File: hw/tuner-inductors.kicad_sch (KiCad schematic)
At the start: 23 parts, among them K7713 G5Q-14-05, K7714 G5Q-14-05, K7715 G5Q-14-05, K7716 G5Q-14-05, K7717 G5Q-14-05, K7718 G5Q-14-05, K7719 G5Q-14-05, U7745 TPIC6C595PWR

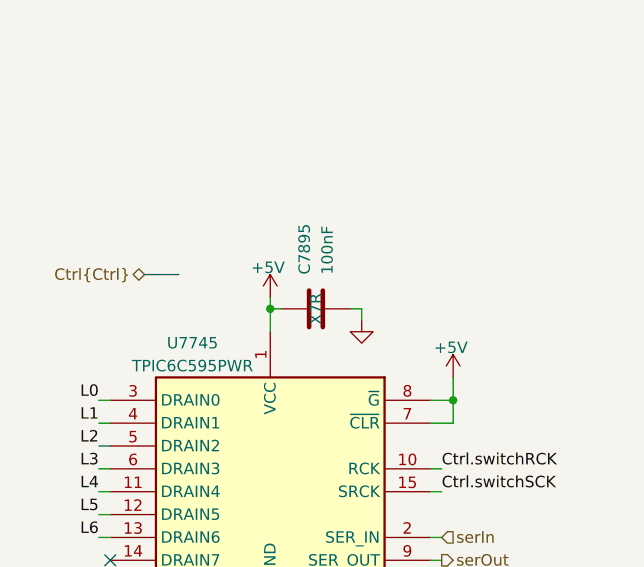
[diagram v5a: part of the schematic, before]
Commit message: All symbols and footprints seem right now, and schematic again imports into PCB without error
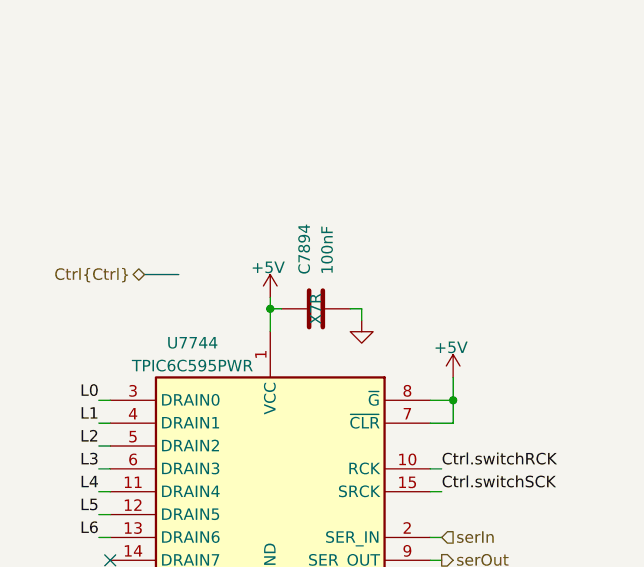
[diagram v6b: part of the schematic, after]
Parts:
- renumbered C7895 to C7894, U7745 to U7744
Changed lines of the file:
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@@
 		(dnp no)
 		(fields_autoplaced yes)
-		(property "Reference" "#PWR07990"
+		(property "Reference" "#PWR07989"
 			(at 39.37 205.74 0)
 			(effects
@@
 			(project "NexRig"
 				(path "/8ae46c04-d01a-4756-8774-512b694bfaff/2406d03c-531b-4eaf-8b4b-4b266b9d0f2b/99bbdde6-e23e-4e3f-9a6c-8b2d863ddc64/99065376-3804-4997-bf5b-41fcd6e501f1"
-					(reference "#PWR07990")
+					(reference "#PWR07989")
 					(unit 1)
 				)
@@
 		(on_board yes)
 		(dnp no)
-		(property "Reference" "#PWR07995"
+		(property "Reference" "#PWR07994"
 			(at 149.86 68.58 0)
 			(effects
@@
 			(project "NexRig"
 				(path "/8ae46c04-d01a-4756-8774-512b694bfaff/2406d03c-531b-4eaf-8b4b-4b266b9d0f2b/99bbdde6-e23e-4e3f-9a6c-8b2d863ddc64/99065376-3804-4997-bf5b-41fcd6e501f1"
-					(reference "#PWR07995")
+					(reference "#PWR07994")
 					(unit 1)
 				)
@@
 		(dnp no)
 		(fields_autoplaced yes)
-		(property "Reference" "#PWR07991"
+		(property "Reference" "#PWR07990"
 			(at 49.53 170.18 0)
 			(effects
@@
 			(project "NexRig"
 				(path "/8ae46c04-d01a-4756-8774-512b694bfaff/2406d03c-531b-4eaf-8b4b-4b266b9d0f2b/99bbdde6-e23e-4e3f-9a6c-8b2d863ddc64/99065376-3804-4997-bf5b-41fcd6e501f1"
-					(reference "#PWR07991")
+					(reference "#PWR07990")
 					(unit 1)
 				)
@@
 		(on_board yes)
 		(dnp no)
-		(property "Reference" "#PWR07992"
+		(property "Reference" "#PWR07991"
 			(at 59.69 173.99 0)
 			(effects
@@
 			(project "NexRig"
 				(path "/8ae46c04-d01a-4756-8774-512b694bfaff/2406d03c-531b-4eaf-8b4b-4b266b9d0f2b/99bbdde6-e23e-4e3f-9a6c-8b2d863ddc64/99065376-3804-4997-bf5b-41fcd6e501f1"
-					(reference "#PWR07992")
+					(reference "#PWR07991")
 					(unit 1)
 				)
@@
 		(on_board yes)
 		(dnp no)
-		(property "Reference" "C7895"
+		(property "Reference" "C7894"
 			(at 43.1799 158.75 0)
 			(effects
@@
 			(project "NexRig"
 				(path "/8ae46c04-d01a-4756-8774-512b694bfaff/2406d03c-531b-4eaf-8b4b-4b266b9d0f2b/99bbdde6-e23e-4e3f-9a6c-8b2d863ddc64/99065376-3804-4997-bf5b-41fcd6e501f1"
-					(reference "C7895")
+					(reference "C7894")
 					(unit 1)
 				)
@@
 		(on_board yes)
 		(dnp no)
-		(property "Reference" "U7745"
+		(property "Reference" "U7744"
 			(at 30.734 166.37 0)
 			(effects
@@
 			(project "NexRig"
 				(path "/8ae46c04-d01a-4756-8774-512b694bfaff/2406d03c-531b-4eaf-8b4b-4b266b9d0f2b/99bbdde6-e23e-4e3f-9a6c-8b2d863ddc64/99065376-3804-4997-bf5b-41fcd6e501f1"
-					(reference "U7745")
+					(reference "U7744")
 					(unit 1)
 				)
@@
 		(on_board yes)
 		(dnp no)
-		(property "Reference" "#PWR07989"
+		(property "Reference" "#PWR07988"
 			(at 39.37 165.1 0)
 			(effects
@@
 			(project "NexRig"
 				(path "/8ae46c04-d01a-4756-8774-512b694bfaff/2406d03c-531b-4eaf-8b4b-4b266b9d0f2b/99bbdde6-e23e-4e3f-9a6c-8b2d863ddc64/99065376-3804-4997-bf5b-41fcd6e501f1"
-					(reference "#PWR07989")
+					(reference "#PWR07988")
 					(unit 1)
 				)
@@
 		(on_board yes)
 		(dnp no)
-		(property "Reference" "#PWR07998"
+		(property "Reference" "#PWR07997"
 			(at 226.06 68.58 0)
 			(effects
@@
 			(project "NexRig"
 				(path "/8ae46c04-d01a-4756-8774-512b694bfaff/2406d03c-531b-4eaf-8b4b-4b266b9d0f2b/99bbdde6-e23e-4e3f-9a6c-8b2d863ddc64/99065376-3804-4997-bf5b-41fcd6e501f1"
-					(reference "#PWR07998")
+					(reference "#PWR07997")
 					(unit 1)
 				)
@@
 		(on_board yes)
 		(dnp no)
-		(property "Reference" "#PWR07996"
+		(property "Reference" "#PWR07995"
 			(at 175.26 68.58 0)
 			(effects
@@
 			(project "NexRig"
 				(path "/8ae46c04-d01a-4756-8774-512b694bfaff/2406d03c-531b-4eaf-8b4b-4b266b9d0f2b/99bbdde6-e23e-4e3f-9a6c-8b2d863ddc64/99065376-3804-4997-bf5b-41fcd6e501f1"
-					(reference "#PWR07996")
+					(reference "#PWR07995")
 					(unit 1)
 				)
@@
 		(on_board yes)
 		(dnp no)
-		(property "Reference" "#PWR07999"
+		(property "Reference" "#PWR07998"
 			(at 251.46 68.58 0)
 			(effects
@@
 			(project "NexRig"
 				(path "/8ae46c04-d01a-4756-8774-512b694bfaff/2406d03c-531b-4eaf-8b4b-4b266b9d0f2b/99bbdde6-e23e-4e3f-9a6c-8b2d863ddc64/99065376-3804-4997-bf5b-41fcd6e501f1"
-					(reference "#PWR07999")
+					(reference "#PWR07998")
 					(unit 1)
 				)
@@
 		(on_board yes)
 		(dnp no)
-		(property "Reference" "#PWR07994"
+		(property "Reference" "#PWR07993"
 			(at 124.46 68.58 0)
 			(effects
@@
 			(project "NexRig"
 				(path "/8ae46c04-d01a-4756-8774-512b694bfaff/2406d03c-531b-4eaf-8b4b-4b266b9d0f2b/99bbdde6-e23e-4e3f-9a6c-8b2d863ddc64/99065376-3804-4997-bf5b-41fcd6e501f1"
-					(reference "#PWR07994")
+					(reference "#PWR07993")
 					(unit 1)
 				)
@@
 		(on_board yes)
 		(dnp no)
-		(property "Reference" "#PWR07993"
+		(property "Reference" "#PWR07992"
 			(at 99.06 68.58 0)
 			(effects
@@
 			(project "NexRig"
 				(path "/8ae46c04-d01a-4756-8774-512b694bfaff/2406d03c-531b-4eaf-8b4b-4b266b9d0f2b/99bbdde6-e23e-4e3f-9a6c-8b2d863ddc64/99065376-3804-4997-bf5b-41fcd6e501f1"
-					(reference "#PWR07993")
+					(reference "#PWR07992")
 					(unit 1)
 				)
@@
 		(on_board yes)
 		(dnp no)
-		(property "Reference" "#PWR07997"
+		(property "Reference" "#PWR07996"
 			(at 200.66 68.58 0)
 			(effects
@@
 			(project "NexRig"
 				(path "/8ae46c04-d01a-4756-8774-512b694bfaff/2406d03c-531b-4eaf-8b4b-4b266b9d0f2b/99bbdde6-e23e-4e3f-9a6c-8b2d863ddc64/99065376-3804-4997-bf5b-41fcd6e501f1"
-					(reference "#PWR07997")
+					(reference "#PWR07996")
 					(unit 1)
 				)

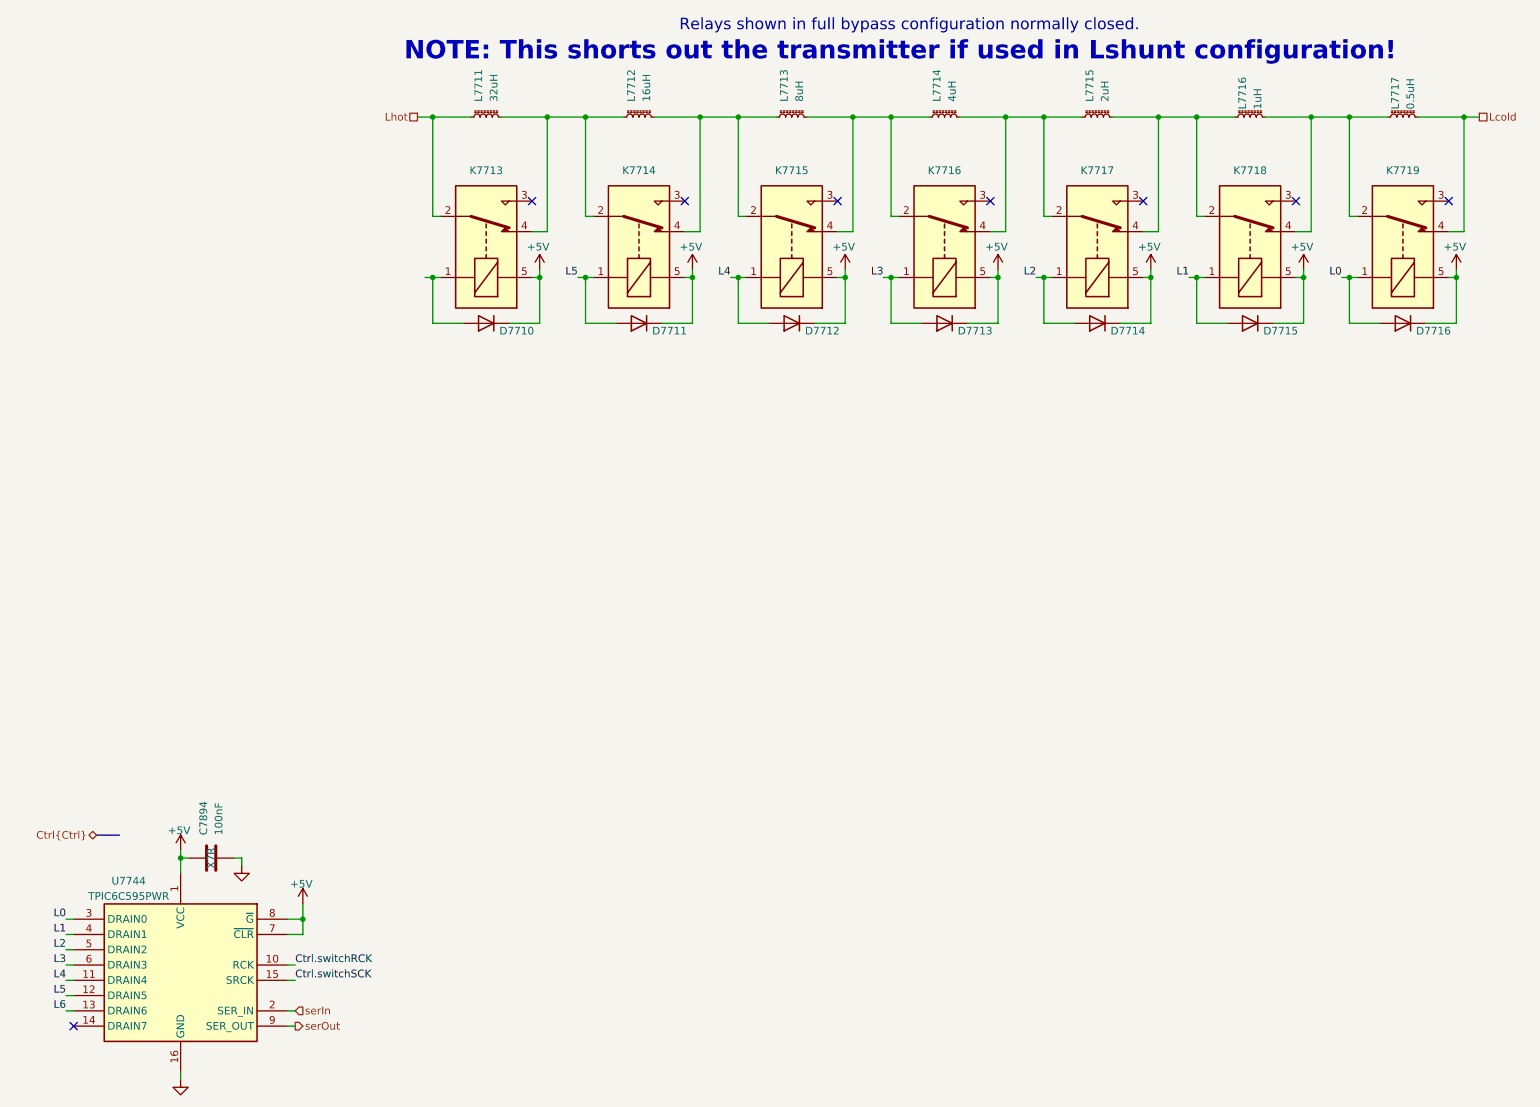
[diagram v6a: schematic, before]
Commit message: About to switch to series-L + shunt-C fore/aft PI network config for antenna tuner
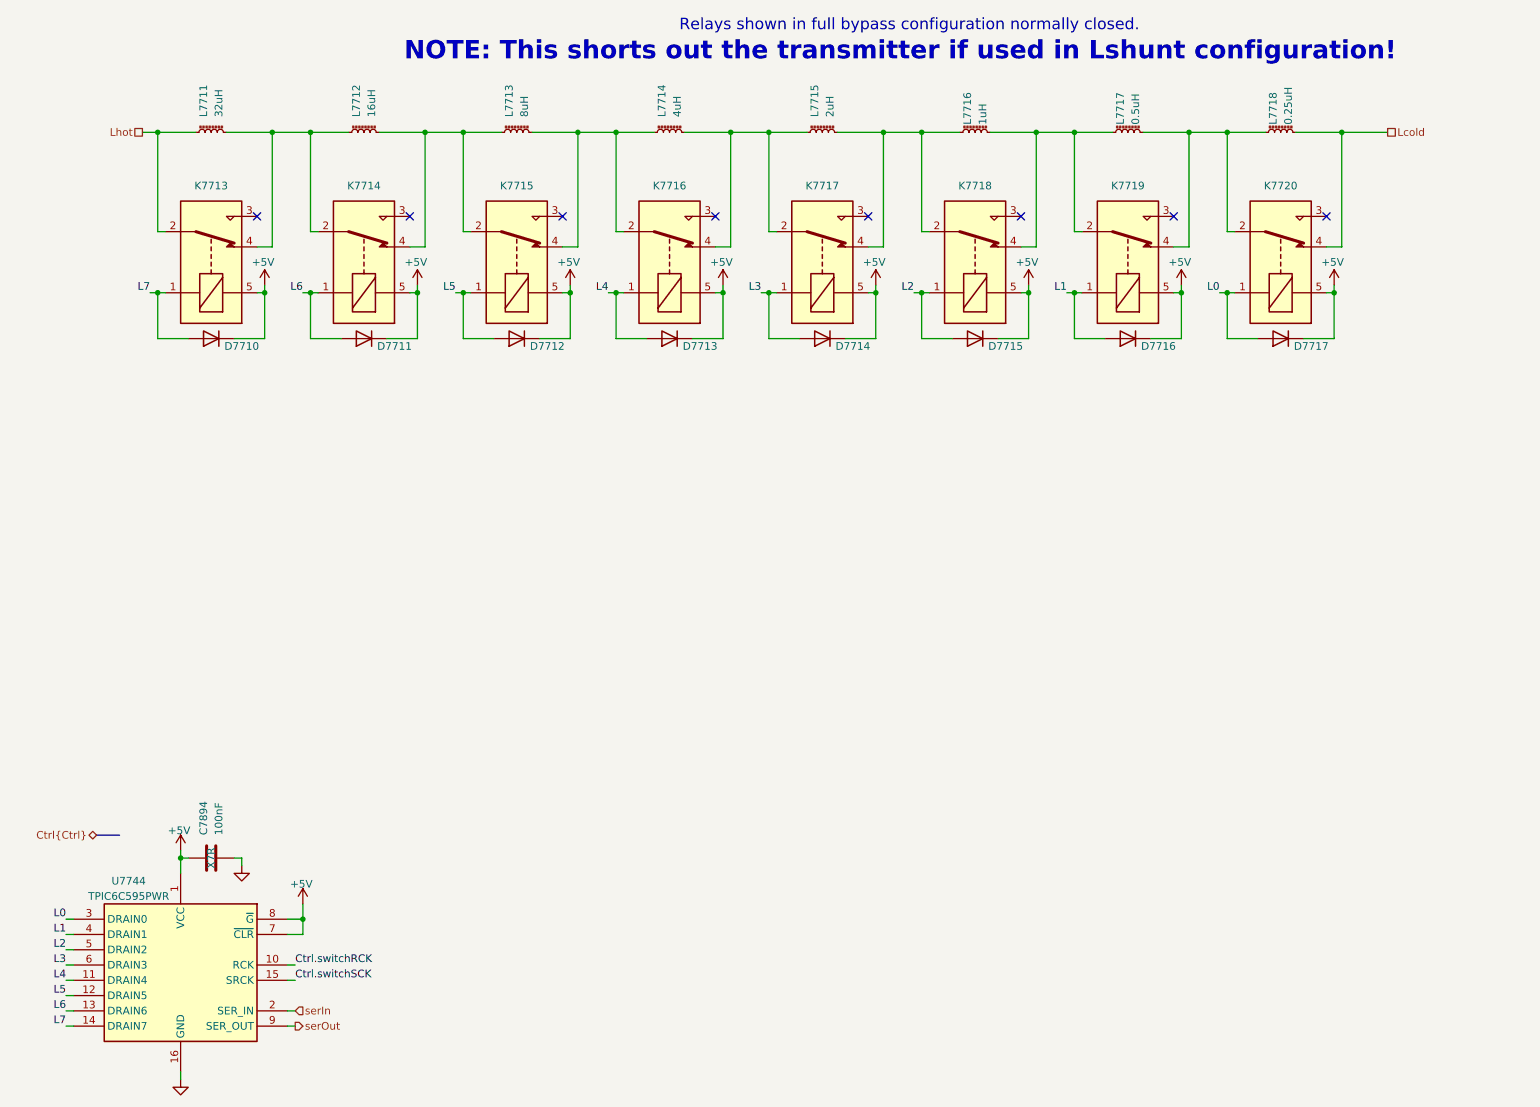
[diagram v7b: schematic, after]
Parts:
- added D7717: 1N4148W, Diode_SMD:D_SOD-123, symbol Diode:1N4148W
- added K7720: G5Q-14-05, Relay_THT:Relay_SPDT_Omron-G5Q-1, symbol Relay:G5Q-1
- added L7718: 0.25uH, Library:T50-toroid-1-rolling-tire, symbol Device:L_Ferrite_Small
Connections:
- net +5V: now also D7717.1 (K), K7720.5
- net L0: now also D7717.2 (A), K7720.1; no longer D7716.2 (A), K7719.1
- net L1: now also D7716.2 (A), K7719.1; no longer D7715.2 (A), K7718.1
- net L2: now also D7715.2 (A), K7718.1; no longer D7714.2 (A), K7717.1
- net L3: now also D7714.2 (A), K7717.1; no longer D7713.2 (A), K7716.1
- net L4: now also D7713.2 (A), K7716.1; no longer D7712.2 (A), K7715.1
- net L5: now also D7712.2 (A), K7715.1; no longer D7711.2 (A), K7714.1
- net L6: now also D7711.2 (A), K7714.1
- net Lcold: now also K7720.4, L7718.2; no longer K7719.4, L7717.2
- net L7: now reaches D7710.2 (A), K7713.1
- net L7: now also U7744.14 (DRAIN7)
- new net: K7719.4, K7720.2, L7717.2, L7718.1
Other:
- moved on the sheet: D7710, D7711, D7712, D7713, D7714, D7715, D7716, K7713, K7714, K7715, K7716, K7717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

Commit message: I'm thinking I might make a NexRx with just the rx portion of this design first to test my skills and capabilities.
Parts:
- renumbered C7894 to C7893, D7710 to D7707, D7711 to D7708, D7712 to D7709, D7713 to D7710, D7714 to D7711, D7715 to D7712, D7716 to D7713, D7717 to D7714, K7713 to K7710, K7714 to K7711, K7715 to K7712, K7716 to K7713, K7717 to K7714, K7718 to K7715, K7719 to K7716, K7720 to K7717
